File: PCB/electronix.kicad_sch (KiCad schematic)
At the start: 132 parts, among them IC1 ICM-20602, IC2 AP9101CK6-ANTRG1, IC3 DRV8210DRLR, IC4 DRV8210DRLR, IC5 LM66200DRLR, J1 USB-C 6pin, J2 PRG, M1 N20, M2 N20, Q1 UMH3N FHA, Q2 dual NMOS, Q3 dual NMOS, Q4 Phototransistor, Q5 Phototransistor, Q6 dual NMOS, Q7 Phototransistor, Q8 Phototransistor, SW1 side slide, SW2 RESET, SW3 START, U1 MCP73213-A6SI/MF, U2 ESP32-WROOM-32, U3 LMR51420YDDRCR

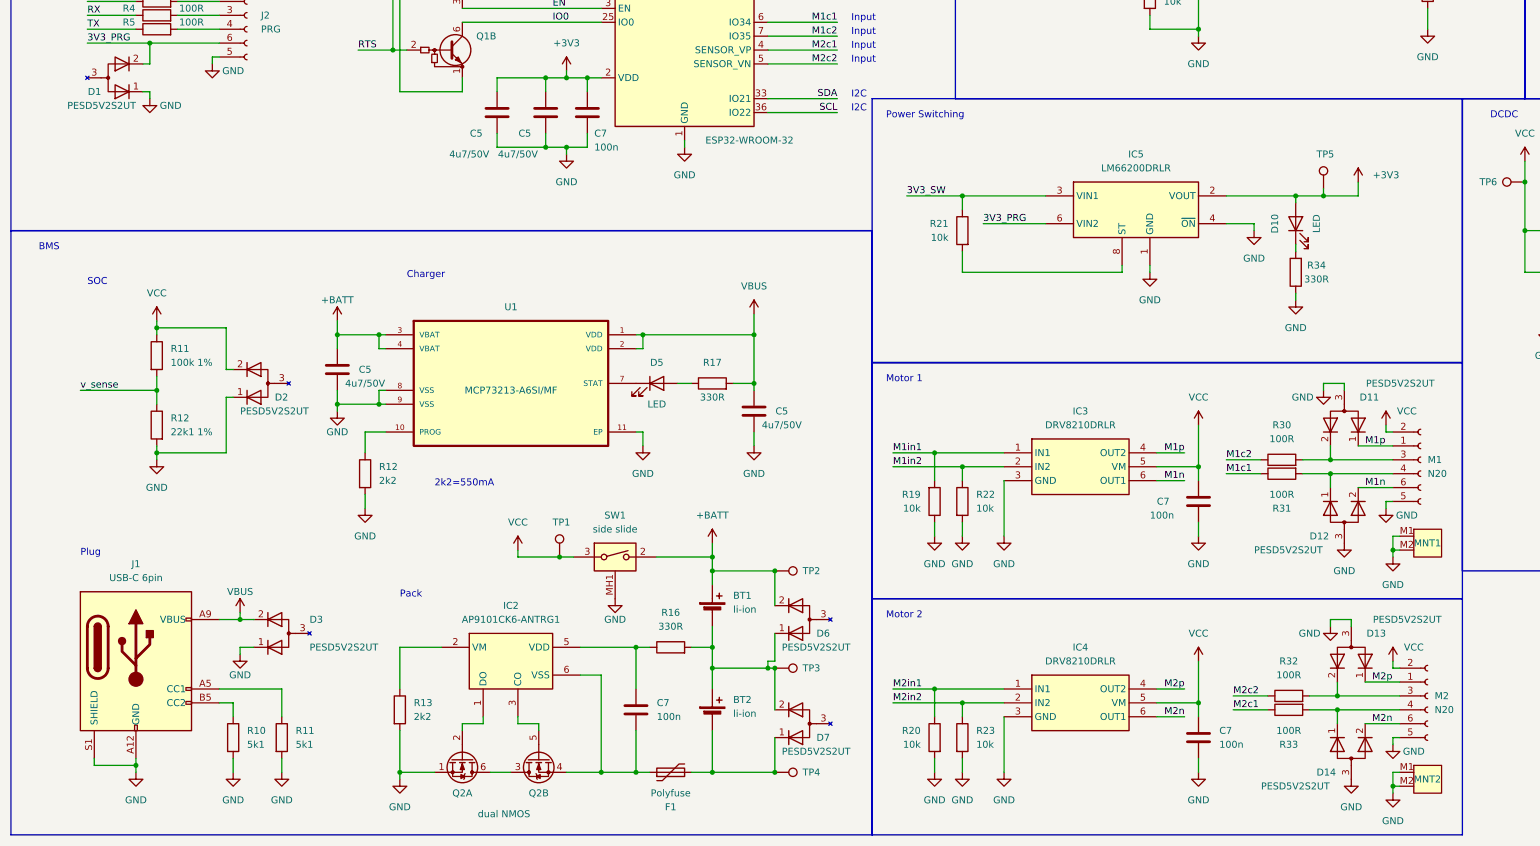
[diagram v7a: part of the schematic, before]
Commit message: ESD layout edits Add TVS part numbers
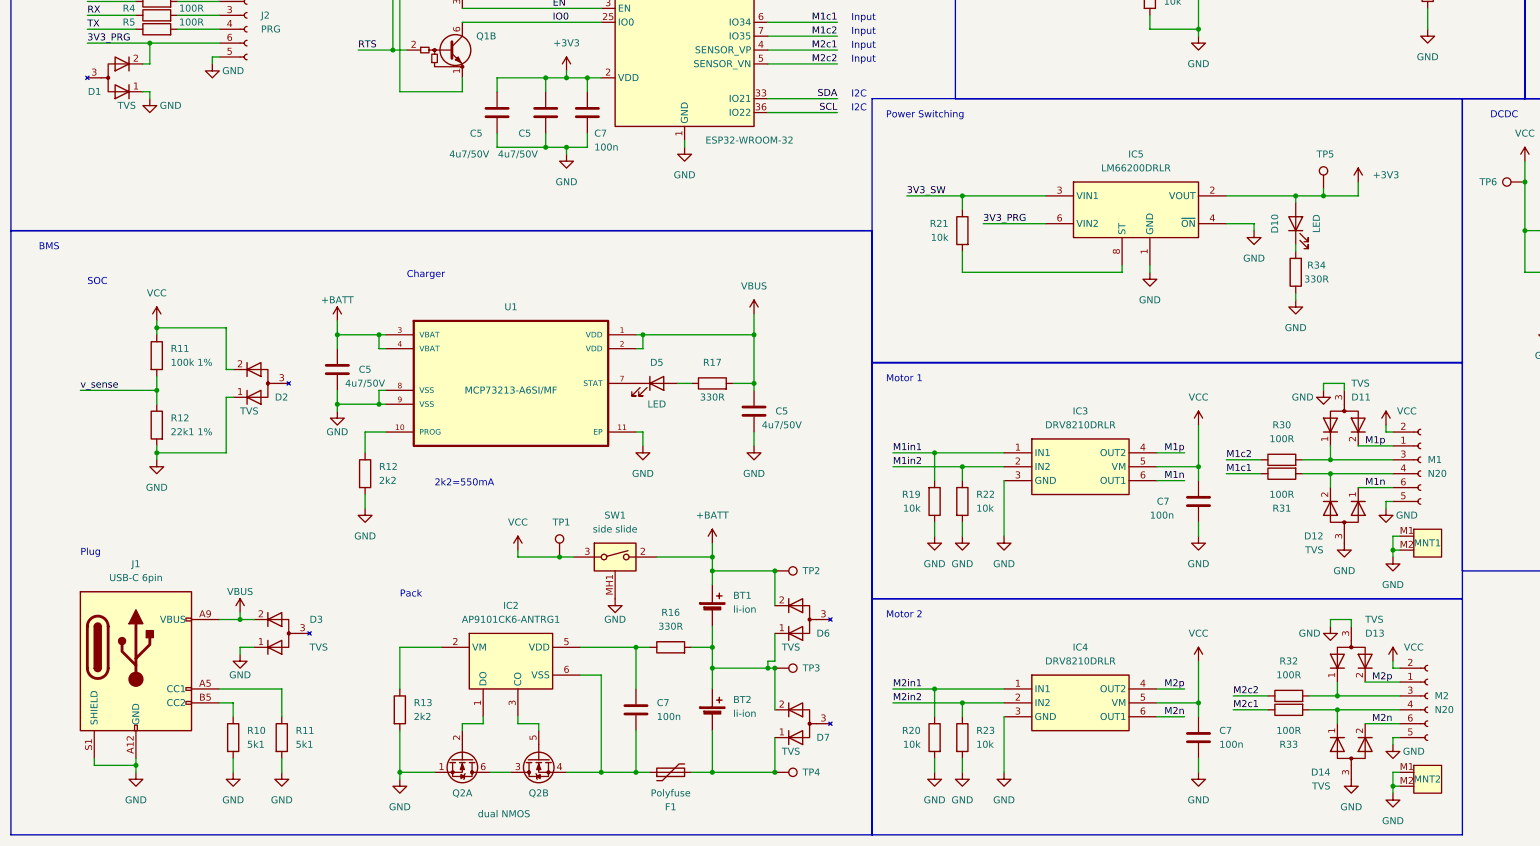
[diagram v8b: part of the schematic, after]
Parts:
- D1, D11, D12, D13, D14, D2, D3, D6, D7: value PESD5V2S2UT -> TVS; Mouser Part Number (none) -> 863-MMBZ15VALT1G
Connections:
- net M1n: now also D12.1 (K); no longer D12.2 (K)
- net M1p: now also D11.2 (K); no longer D11.1 (K)
- net M2p: now also D13.2 (K); no longer D13.1 (K)
- net at M2.3 (Pin_3), R32.2: now also D13.1 (K); no longer D13.2 (K)
- net at M1.3 (Pin_3), R30.2: now also D11.1 (K); no longer D11.2 (K)
- net at M1.4 (Pin_4), R31.2: now also D12.2 (K); no longer D12.1 (K)
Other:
- moved on the sheet: D11, D12, D13
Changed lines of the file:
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@@
       (effects (font (size 1.27 1.27)) (justify right))
     )
-    (property "Value" "PESD5V2S2UT" (at 162.56 243.84 0)
+    (property "Value" "TVS" (at 162.56 243.84 0)
       (effects (font (size 1.27 1.27)) (justify right))
     )
@@
       (effects (font (size 1.27 1.27)) hide)
     )
+    (property "Mouser Part Number" "863-MMBZ15VALT1G" (at 166.37 238.76 0)
+      (effects (font (size 1.27 1.27)) hide)
+    )
     (pin "1")
     (pin "2")
@@
   (symbol (lib_name "D_Dual_CommonAnode_KKA_Parallel_3") (lib_id "Device:D_Dual_CommonAnode_KKA_Parallel") (at 266.7 262.89 90) (unit 1)
     (in_bom yes) (on_board yes) (dnp no)
-    (property "Reference" "D14" (at 260.35 266.7 90)
-      (effects (font (size 1.27 1.27)) (justify right))
+    (property "Reference" "D14" (at 262.89 266.7 90)
+      (effects (font (size 1.27 1.27)) (justify left))
     )
-    (property "Value" "PESD5V2S2UT" (at 250.19 269.24 90)
-      (effects (font (size 1.27 1.27)) (justify right))
+    (property "Value" "TVS" (at 262.89 269.24 90)
+      (effects (font (size 1.27 1.27)) (justify left))
     )
     (property "Footprint" "Package_TO_SOT_SMD:SOT-23-3" (at 266.7 264.16 0)
@@
       (effects (font (size 1.27 1.27)) hide)
     )
+    (property "Mouser Part Number" "863-MMBZ15VALT1G" (at 266.7 262.89 0)
+      (effects (font (size 1.27 1.27)) hide)
+    )
     (pin "1")
     (pin "2")
@@
     )
   )
-  (symbol (lib_name "D_Dual_CommonAnode_KKA_Parallel_3") (lib_id "Device:D_Dual_CommonAnode_KKA_Parallel") (at 265.43 219.71 90) (unit 1)
+  (symbol (lib_name "D_Dual_CommonAnode_KKA_Parallel_3") (lib_id "Device:D_Dual_CommonAnode_KKA_Parallel") (at 265.43 219.71 270) (mirror x) (unit 1)
     (in_bom yes) (on_board yes) (dnp no)
-    (property "Reference" "D12" (at 259.08 223.52 90)
+    (property "Reference" "D12" (at 261.62 223.52 90)
       (effects (font (size 1.27 1.27)) (justify right))
     )
-    (property "Value" "PESD5V2S2UT" (at 248.92 226.06 90)
+    (property "Value" "TVS" (at 261.62 226.06 90)
       (effects (font (size 1.27 1.27)) (justify right))
     )
@@
       (effects (font (size 1.27 1.27)) hide)
     )
+    (property "Mouser Part Number" "863-MMBZ15VALT1G" (at 265.43 219.71 0)
+      (effects (font (size 1.27 1.27)) hide)
+    )
     (pin "1")
     (pin "2")
@@
       (effects (font (size 1.27 1.27)) (justify right))
     )
-    (property "Value" "PESD5V2S2UT" (at 63.5 200.66 0)
+    (property "Value" "TVS" (at 63.5 200.66 0)
       (effects (font (size 1.27 1.27)) (justify right))
     )
@@
       (effects (font (size 1.27 1.27)) hide)
     )
+    (property "Mouser Part Number" "863-MMBZ15VALT1G" (at 67.31 195.58 0)
+      (effects (font (size 1.27 1.27)) hide)
+    )
     (pin "1")
     (pin "2")
@@
     )
   )
-  (symbol (lib_name "D_Dual_CommonAnode_KKA_Parallel_3") (lib_id "Device:D_Dual_CommonAnode_KKA_Parallel") (at 265.43 201.93 270) (unit 1)
+  (symbol (lib_name "D_Dual_CommonAnode_KKA_Parallel_3") (lib_id "Device:D_Dual_CommonAnode_KKA_Parallel") (at 265.43 201.93 90) (mirror x) (unit 1)
     (in_bom yes) (on_board yes) (dnp no)
-    (property "Reference" "D11" (at 271.78 198.12 90)
+    (property "Reference" "D11" (at 266.7 198.12 90)
       (effects (font (size 1.27 1.27)) (justify right))
     )
-    (property "Value" "PESD5V2S2UT" (at 281.94 195.58 90)
+    (property "Value" "TVS" (at 266.7 195.58 90)
       (effects (font (size 1.27 1.27)) (justify right))
     )
@@
       (effects (font (size 1.27 1.27)) hide)
     )
+    (property "Mouser Part Number" "863-MMBZ15VALT1G" (at 265.43 201.93 0)
+      (effects (font (size 1.27 1.27)) hide)
+    )
     (pin "1")
     (pin "2")
@@
       (effects (font (size 1.27 1.27)) (justify right))
     )
-    (property "Value" "PESD5V2S2UT" (at 76.2 243.84 0)
+    (property "Value" "TVS" (at 76.2 243.84 0)
       (effects (font (size 1.27 1.27)) (justify right))
     )
@@
       (effects (font (size 1.27 1.27)) hide)
     )
+    (property "Mouser Part Number" "863-MMBZ15VALT1G" (at 71.12 241.3 0)
+      (effects (font (size 1.27 1.27)) hide)
+    )
     (pin "1")
     (pin "2")
@@
     )
   )
-  (symbol (lib_name "D_Dual_CommonAnode_KKA_Parallel_3") (lib_id "Device:D_Dual_CommonAnode_KKA_Parallel") (at 266.7 245.11 270) (unit 1)
+  (symbol (lib_name "D_Dual_CommonAnode_KKA_Parallel_3") (lib_id "Device:D_Dual_CommonAnode_KKA_Parallel") (at 266.7 245.11 90) (mirror x) (unit 1)
     (in_bom yes) (on_board yes) (dnp no)
-    (property "Reference" "D13" (at 273.05 241.3 90)
+    (property "Reference" "D13" (at 269.24 241.3 90)
       (effects (font (size 1.27 1.27)) (justify right))
     )
-    (property "Value" "PESD5V2S2UT" (at 283.21 238.76 90)
+    (property "Value" "TVS" (at 269.24 238.76 90)
       (effects (font (size 1.27 1.27)) (justify right))
     )
@@
       (effects (font (size 1.27 1.27)) hide)
     )
+    (property "Mouser Part Number" "863-MMBZ15VALT1G" (at 266.7 245.11 0)
+      (effects (font (size 1.27 1.27)) hide)
+    )
     (pin "1")
     (pin "2")
@@
       (effects (font (size 1.27 1.27)) (justify right))
     )
-    (property "Value" "PESD5V2S2UT" (at 162.56 262.89 0)
+    (property "Value" "TVS" (at 162.56 262.89 0)
       (effects (font (size 1.27 1.27)) (justify right))
     )
@@
       (effects (font (size 1.27 1.27)) hide)
     )
+    (property "Mouser Part Number" "863-MMBZ15VALT1G" (at 166.37 257.81 0)
+      (effects (font (size 1.27 1.27)) hide)
+    )
     (pin "1")
     (pin "2")
@@
       (effects (font (size 1.27 1.27)) (justify right))
     )
-    (property "Value" "PESD5V2S2UT" (at 44.45 144.78 0)
+    (property "Value" "TVS" (at 44.45 144.78 0)
       (effects (font (size 1.27 1.27)) (justify right))
     )
@@
       (effects (font (size 1.27 1.27)) hide)
     )
+    (property "Mouser Part Number" "863-MMBZ15VALT1G" (at 40.64 139.7 0)
+      (effects (font (size 1.27 1.27)) hide)
+    )
